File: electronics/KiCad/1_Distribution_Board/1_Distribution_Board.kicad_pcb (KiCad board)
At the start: 2 copper layers, 130 x 120 mm, 192 parts, among them CN1 HC-5264-3A, CN2 HC-5264-3A, J1 JST VH, J10 Generic 2.54mm, J11 Generic 2.54mm, J12 Conn_01x06, J13 Conn_01x10, J14 2.54-1*4P母, J15 2.54-1*4P母, J16 PM254V-11-06-H85, J17 Conn_02x08_Odd_Even, J18 PM254V-11-06-H85, J19 2.54-1*4P母, J2 JST VH, J20 2.54-1*4P母, J21 Jumper Pins, J22 Jumper Pins, J23 JST PH, J24 Generic 2.54mm, J25 Jumper Pins, J26 Jumper Pins, J27 JST PH, J28 Generic 2.54mm, J29 Jumper Pins, J3 JST VH, J30 Jumper Pins, J31 JST PH, J32 Generic 2.54mm, J33 Jumper Pins, J34 Jumper Pins, J35 JST PH, J36 Generic 2.54mm, J37 Jumper Pins, J38 Jumper Pins, J39 JST PH, J4 Conn_01x04, J40 Generic 2.54mm, J5 Generic 2.54mm, J6 Generic 2.54mm, J8 Generic 2.54mm, J9 Generic 2.54mm, M1 MountingHole_3.2mm_M3_ISO7380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, P1 Header-Female-2.54_1x8, P10 Header-Female-2.54_1x8, P11 Header-Female-2.54_1x2, P12 Header-Female-2.54_1x8, P13 Header-Female-2.54_1x8, P14 Header-Female-2.54_1x2, P15 Header-Female-2.54_1x8, P2 Header-Female-2.54_1x2, P3 Header-Female-2.54_1x8, P4 Header-Female-2.54_1x8, P5 Header-Female-2.54_1x2, P6 Header-Female-2.54_1x8, P7 Header-Female-2.54_1x8, P8 Header-Female-2.54_1x2, P9 Header-Female-2.54_1x8, Q1 DMG2305UX, Q2 AO3400A, Q3 AO3400A, Q4 AO3400A, Q5 AO3400A, U1 KH-2.54FH-1X20P-H8.5, U2 KH-2.54FH-1X20P-H8.5, U3 R-78C5.0-1.0, U4 R-78B12-2.0, U5 R-78B6.5-1.5, U6 PCA9306, U7 PCA9685PW, Y1 25MHz

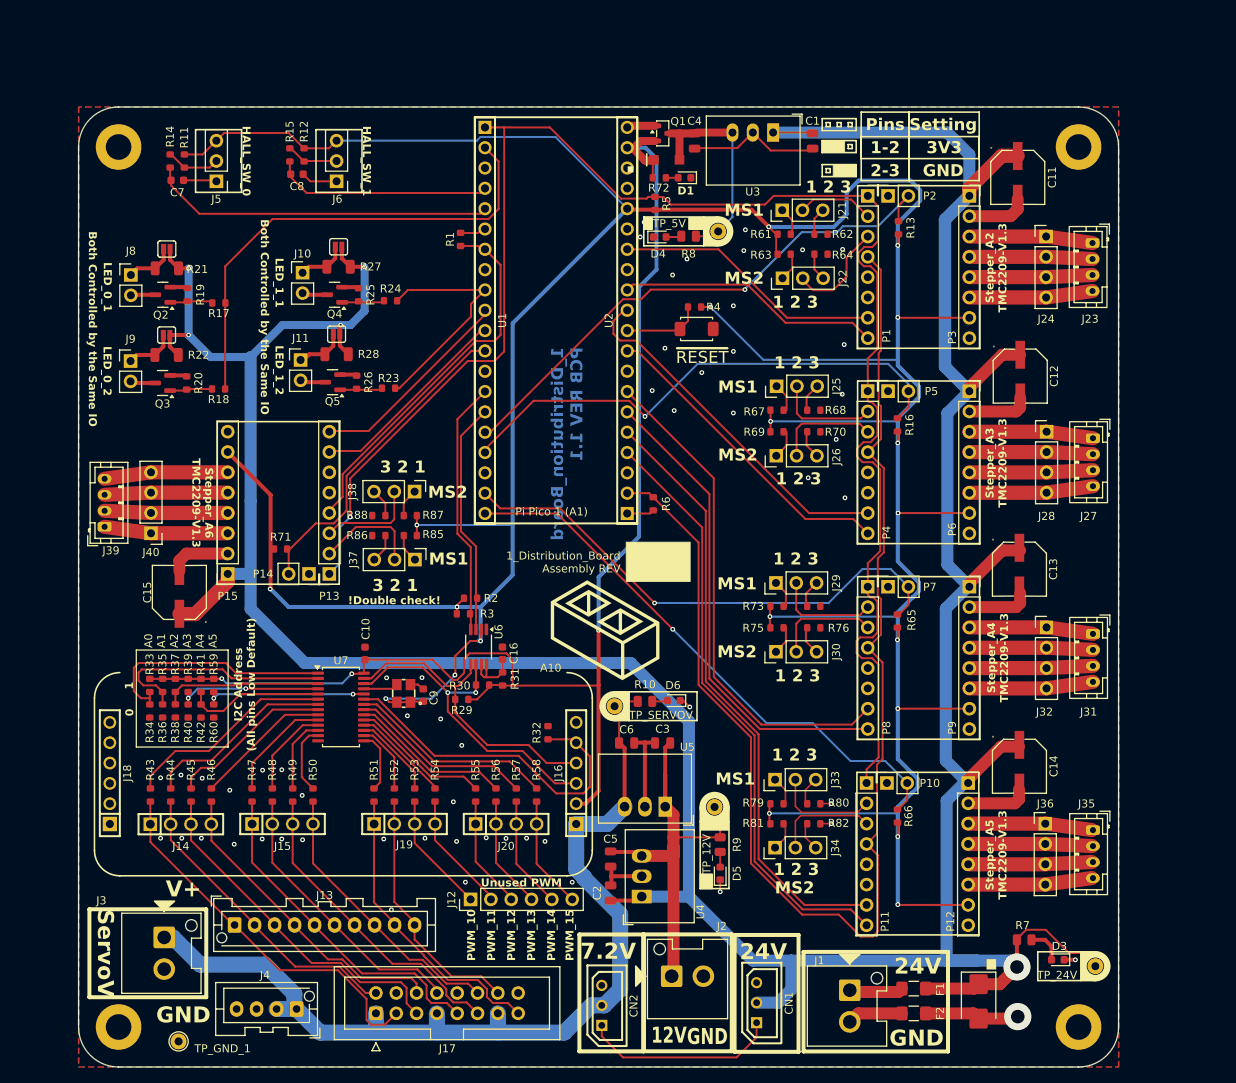
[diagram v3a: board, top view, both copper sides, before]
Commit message: Updated rules to correct errors
Cleaned up rules a bit to prevent false errors.
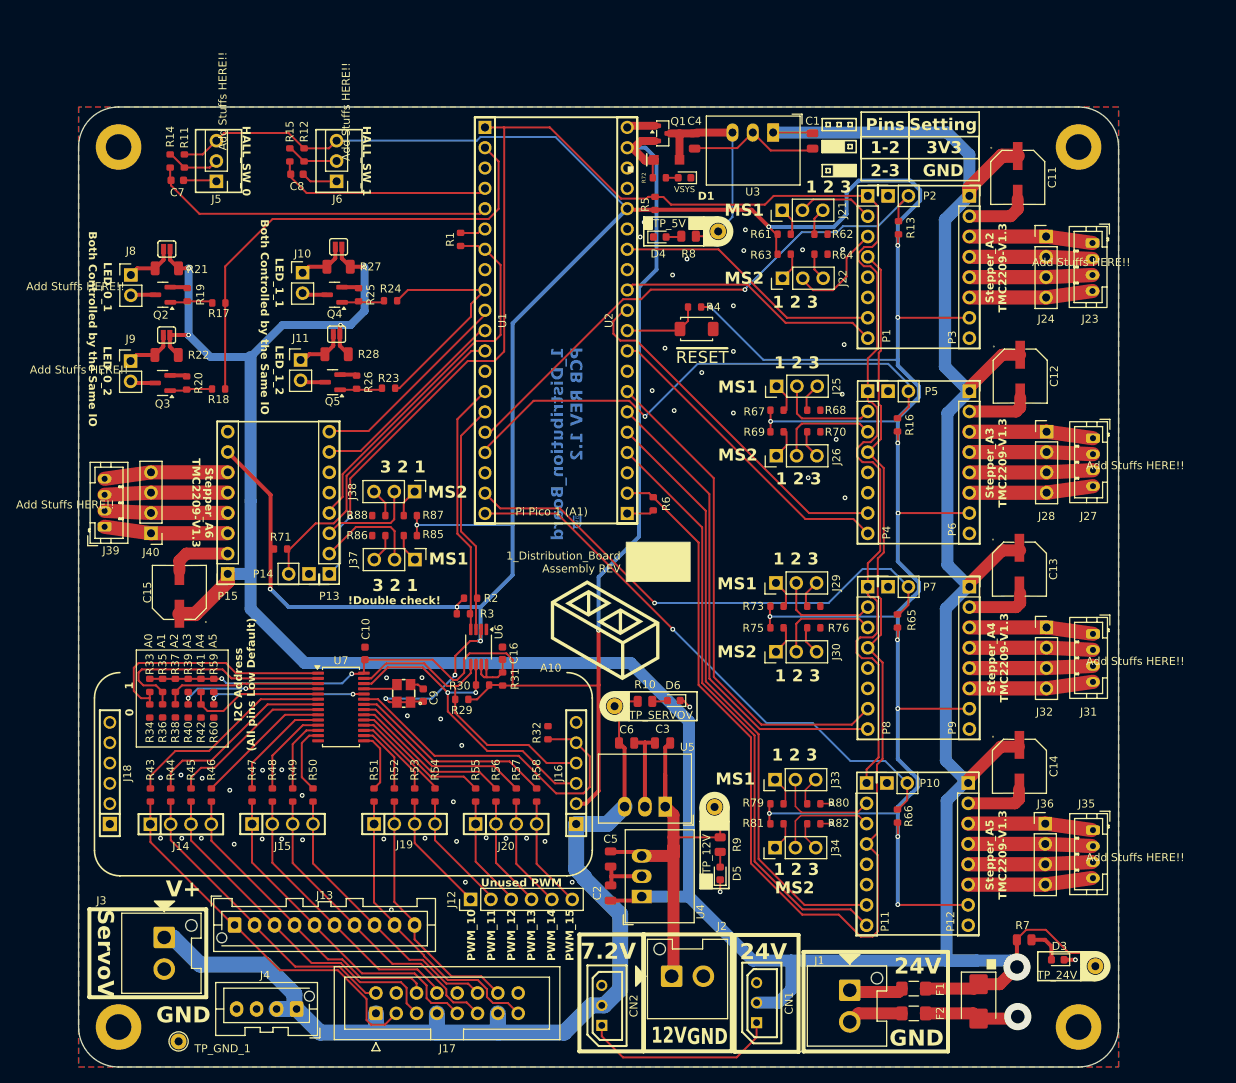
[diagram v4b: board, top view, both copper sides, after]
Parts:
- added JAW: Maker's Mark, JAW:JAW, B.Cu at (87.4, 76.8)
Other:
- board text added: "1_Distribution_Board PCB REV 1.2"
- board text added: "Add Stuffs HERE!!"
- board text added: "VSYS"
- board text removed: "1_Distribution_Board PCB REV 1.1"
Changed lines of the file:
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@@
 	(title_block
 		(title "1_Distribution Board")
-		(date "2026-05-22")
-		(rev "1.1")
+		(date "2026-05-25")
+		(rev "1.2")
 		(company "basically")
 	)
@@
 		(tags "resistor")
 		(property "Reference" "R72"
-			(at -0.0682 1.27 0)
+			(at -1.9304 0 90)
 			(layer "F.SilkS")
 			(effects
 				(font
-					(size 1 1)
+					(size 0.5 0.5)
 					(thickness 0.15)
 				)
@@
 		(tags "resistor")
 		(property "Reference" "R5"
-			(at 0 1.45 90)
+			(at -0.1524 -1.2348 90)
 			(layer "F.SilkS")
 			(effects
@@
 		)
 	)
+	(footprint "JAW:JAW"
+		(layer "B.Cu")
+		(at 87.3824 76.7756 -90)
+		(property "Reference" "JAW"
+			(at 0 0.5 90)
+			(unlocked yes)
+			(layer "B.SilkS")
+			(hide yes)
+			(effects
+				(font
+					(size 1 1)
+					(thickness 0.1)
+				)
+				(justify mirror)
+			)
+		)
+		(property "Value" "Maker's Mark"
+			(at 0 -1 90)
+			(unlocked yes)
+			(layer "B.Fab")
+			(effects
+				(font
+					(size 1 1)
+					(thickness 0.15)
+				)
+				(justify mirror)
+			)
+		)
+		(property "Datasheet" ""
+			(at 0 0 90)
+			(unlocked yes)
+			(layer "B.Fab")
+			(hide yes)
+			(effects
+				(font
+					(size 1 1)
+					(thickness 0.15)
+				)
+				(justify mirror)
+			)
+		)
+		(property "Description" ""
+			(at 0 0 90)
+			(unlocked yes)
+			(layer "B.Fab")
+			(hide yes)
+			(effects
+				(font
+					(size 1 1)
+					(thickness 0.15)
+				)
+				(justify mirror)
+			)
+		)
+		(attr smd)
+		(fp_line
+			(start -0.6604 0.508)
+			(end 0.9144 0.508)
+			(stroke
+				(width 0.2)
+				(type default)
+			)
+			(layer "B.Cu")
+		)
+		(fp_line
+			(start 0.3556 -0.3556)
+			(end -0.6604 -0.3556)
+			(stroke
+				(width 0.2)
+				(type default)
+			)
+			(layer "B.Cu")
+		)
+		(fp_arc
+			(start 0.3556 -0.356264)
+			(mid 0.787732 0.075868)
+			(end 0.3556 0.508)
+			(stroke
+				(width 0.2)
+				(type default)
+			)
+			(layer "B.Cu")
+		)
+		(fp_text user "aw"
+			(at -0.7112 -0.2032 90)
+			(unlocked yes)
+			(layer "B.Cu")
+			(effects
+				(font
+					(size 0.6 0.6)
+					(thickness 0.2)
+				)
+				(justify left bottom mirror)
+			)
+		)
+		(fp_text user "${REFERENCE}"
+			(at 0 -2.5 90)
+			(unlocked yes)
+			(layer "B.Fab")
+			(effects
+				(font
+					(size 1 1)
+					(thickness 0.15)
+				)
+				(justify mirror)
+			)
+		)
+		(embedded_fonts no)
+	)
 	(gr_line
 		(start 89.217 98.875)
@@
 		(layer "Edge.Cuts")
 	)
-	(gr_text "1_Distribution_Board\nPCB REV 1.1"
+	(gr_text "1_Distribution_Board\nPCB REV 1.2"
 		(at 88.15 55 90)
 		(layer "B.Cu")
@@
 		)
 	)
+	(gr_text "Add Stuffs HERE!!"
+		(at 18.904 58.4368 0)
+		(layer "F.SilkS")
+		(effects
+			(font
+				(size 1 1)
+				(thickness 0.1)
+			)
+			(justify left bottom)
+		)
+	)
 	(gr_text "2-3"
 		(at 125.825 32.95 0)
@@
 	)
 	(gr_text "D1"
-		(at 100.8952 35.4752 0)
+		(at 103.4352 36.1356 0)
 		(layer "F.SilkS")
 		(effects
@@
 		)
 	)
+	(gr_text "Add Stuffs HERE!!"
+		(at 59.02 31.75 90)
+		(layer "F.SilkS")
+		(effects
+			(font
+				(size 1 1)
+				(thickness 0.1)
+			)
+			(justify left bottom)
+		)
+	)
+	(gr_text "Add Stuffs HERE!!"
+		(at 17.1768 75.3024 0)
+		(layer "F.SilkS")
+		(effects
+			(font
+				(size 1 1)
+				(thickness 0.1)
+			)
+			(justify left bottom)
+		)
+	)
+	(gr_text "Add Stuffs HERE!!"
+		(at 18.4468 48.0228 0)
+		(layer "F.SilkS")
+		(effects
+			(font
+				(size 1 1)
+				(thickness 0.1)
+			)
+			(justify left bottom)
+		)
+	)
 	(gr_text "Stepper_A6\nTMC2209-V1.3"
 		(at 39.1 74.4896 270)
@@
 		)
 	)
+	(gr_text "Add Stuffs HERE!!"
+		(at 150.925 70.4 0)
+		(layer "F.SilkS")
+		(effects
+			(font
+				(size 1 1)
+				(thickness 0.1)
+			)
+			(justify left bottom)
+		)
+	)
 	(gr_text "3V3"
 		(at 133.2 30.075 0)
@@
 		)
 	)
+	(gr_text "Add Stuffs HERE!!"
+		(at 150.925 119.39 0)
+		(layer "F.SilkS")
+		(effects
+			(font
+				(size 1 1)
+				(thickness 0.1)
+			)
+			(justify left bottom)
+		)
+	)
 	(gr_text "MS2"
 		(at 108.2 46.4 0)
@@
 		)
 	)
+	(gr_text "VSYS"
+		(at 99.422 35.7292 0)
+		(layer "F.SilkS" knockout)
+		(effects
+			(font
+				(size 0.75 0.75)
+				(thickness 0.2)
+			)
+			(justify left bottom)
+		)
+	)
 	(gr_text "LED_0_1"
 		(at 28.032 47.498 270)
@@
 		)
 	)
+	(gr_text "Add Stuffs HERE!!"
+		(at 43.605 30.425 90)
+		(layer "F.SilkS")
+		(effects
+			(font
+				(size 1 1)
+				(thickness 0.1)
+			)
+			(justify left bottom)
+		)
+	)
 	(gr_text "0"
 		(at 31.9596 101.1596 90)
@@
 		)
 	)
+	(gr_text "Add Stuffs HERE!!"
+		(at 150.925 94.865 0)
+		(layer "F.SilkS")
+		(effects
+			(font
+				(size 1 1)
+				(thickness 0.1)
+			)
+			(justify left bottom)
+		)
+	)
 	(gr_text "."
 		(at 139.1 130.5 0)
@@
 		)
 	)
+	(gr_text "Add Stuffs HERE!!"
+		(at 144.17 45 0)
+		(layer "F.SilkS")
+		(effects
+			(font
+				(size 1 1)
+				(thickness 0.1)
+			)
+			(justify left bottom)
+		)
+	)

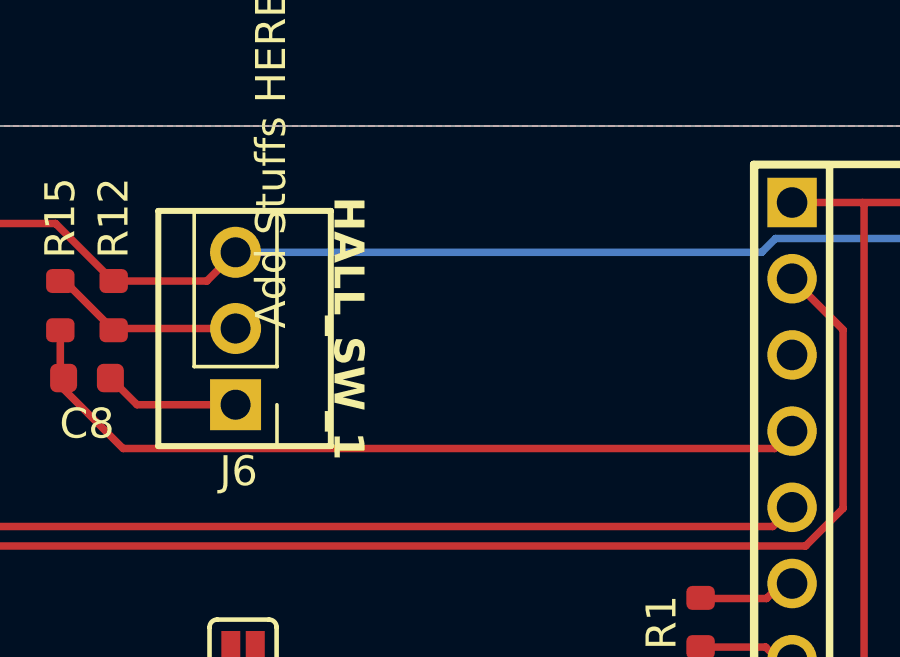
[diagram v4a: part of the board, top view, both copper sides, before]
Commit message: Started work on silk update
Slowly started work on silk update.
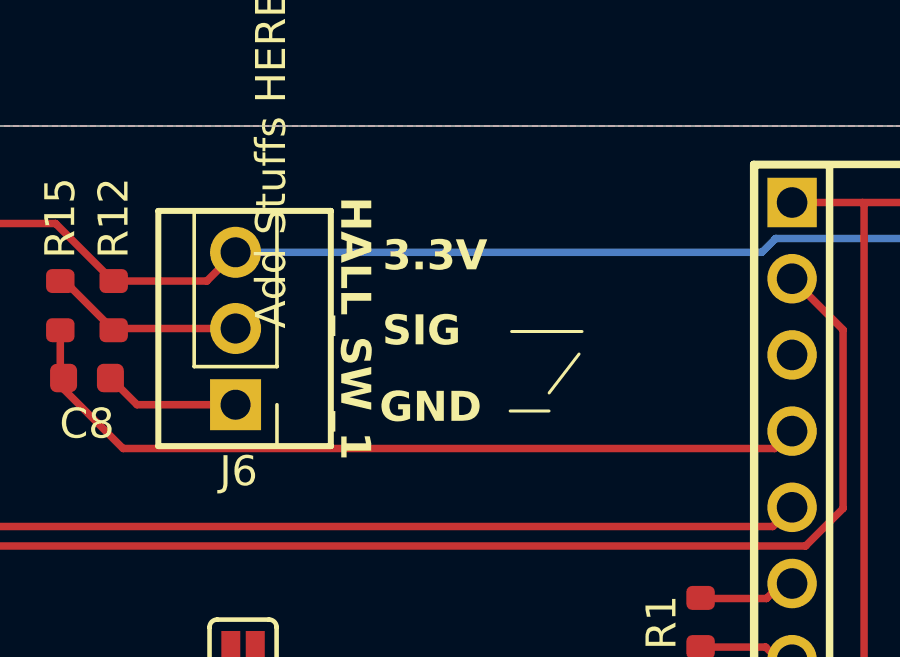
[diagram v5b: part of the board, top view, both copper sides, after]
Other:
- board text added: "3.3V"
- board text added: "SIG"
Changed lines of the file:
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@@
+		(layer "F.SilkS")
+	)
+	(gr_line
+		(start 67.7 33.9)
+		(end 68.7 32.6)
+		(stroke
+			(width 0.1)
+			(type default)
+		)
 		(layer "F.SilkS")
 	)
@@
 		)
 		(fill no)
+		(layer "F.SilkS")
+	)
+	(gr_line
+		(start 66.45 31.85)
+		(end 68.8 31.85)
+		(stroke
+			(width 0.1)
+			(type default)
+		)
 		(layer "F.SilkS")
 	)
@@
 		)
 		(fill no)
+		(layer "F.SilkS")
+	)
+	(gr_line
+		(start 67.7 34.5)
+		(end 66.4 34.5)
+		(stroke
+			(width 0.1)
+			(type default)
+		)
 		(layer "F.SilkS")
 	)
@@
 	)
 	(gr_text "HALL_SW_1"
-		(at 60.425 31.75 270)
+		(at 60.65 31.75 270)
 		(layer "F.SilkS" knockout)
 		(effects
@@
 				(bold yes)
 			)
+		)
+	)
+	(gr_text "GND\n"
+		(at 63.75 34.95 0)
+		(layer "F.SilkS" knockout)
+		(effects
+			(font
+				(size 1 1)
+				(thickness 0.2)
+				(bold yes)
+			)
+			(justify bottom)
 		)
 	)
@@
 		)
 	)
+	(gr_text "SIG"
+		(at 63.45 32.4 0)
+		(layer "F.SilkS" knockout)
+		(effects
+			(font
+				(size 1 1)
+				(thickness 0.2)
+				(bold yes)
+			)
+			(justify bottom)
+		)
+	)
 	(gr_text "12V"
 		(at 98.8 141.033274 0)
@@
 		)
 	)
+	(gr_text "3.3V"
+		(at 63.9 29.9 0)
+		(layer "F.SilkS" knockout)
+		(effects
+			(font
+				(size 1 1)
+				(thickness 0.2)
+				(bold yes)
+			)
+			(justify bottom)
+		)
+	)
